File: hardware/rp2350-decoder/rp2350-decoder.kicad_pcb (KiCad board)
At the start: 6 copper layers, 19.9 x 8.8 mm, 67 parts, among them J1 SWDIO, J2 SWCLK, J3 5052702412, Q1 DMN2991UDA-7B, Q2 DMN2991UDA-7B, Q3 NST847BPDP6T5G, Q4 NST847BPDP6T5G, Q5 DMN2991UDA-7B, Q6 DMN2991UDA-7B, Q7 DMN2991UDA-7B, Q8 DMN2991UDA-7B, SW1 BOOT, U1 NCS2220AMUT1G, U2 AP63203WU, U3 W25Q128JVPIQ, U4 RP2350A, U5 MAX98357AEWL+T, U6 MD9927, Y1 X252012MMB4SI

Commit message: chore: increase bootsel resistance
chore: add missing heights
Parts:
- R6: value 1K -> 6.8K
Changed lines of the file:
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@@
 			)
 		)
-		(property "Frequency" ""
+		(property "Height" "1.0"
+			(at 0 0 -90)
+			(unlocked yes)
+			(layer "F.Fab")
+			(hide yes)
+			(effects
+				(font
+					(size 1 1)
+					(thickness 0.15)
+				)
+			)
+		)
+		(property "LCSC Part" "C42411119"
 			(at 0 0 -90)
 			(unlocked yes)
@@
 			)
 		)
+		(property "Height" "0.26"
+			(at 0 0 0)
+			(unlocked yes)
+			(layer "F.Fab")
+			(hide yes)
+			(effects
+				(font
+					(size 1 1)
+					(thickness 0.15)
+				)
+			)
+		)
 		(property ki_fp_filters "R_*")
 		(sheetname "Root")
@@
 			)
 		)
-		(property "Frequency" ""
+		(property "Height" "0.26"
 			(at 0 0 90)
 			(unlocked yes)
@@
 			)
 		)
+		(property "Height" "0.26"
+			(at 0 0 0)
+			(unlocked yes)
+			(layer "F.Fab")
+			(hide yes)
+			(effects
+				(font
+					(size 1 1)
+					(thickness 0.15)
+				)
+			)
+		)
 		(property ki_fp_filters "R_*")
 		(sheetname "Root")
@@
 			)
 		)
+		(property "Height" "0.26"
+			(at 0 0 0)
+			(unlocked yes)
+			(layer "F.Fab")
+			(hide yes)
+			(effects
+				(font
+					(size 1 1)
+					(thickness 0.15)
+				)
+			)
+		)
 		(property ki_fp_filters "R_*")
 		(sheetname "Root")
@@
 			)
 		)
+		(property "Height" "0.26"
+			(at 0 0 0)
+			(unlocked yes)
+			(layer "F.Fab")
+			(hide yes)
+			(effects
+				(font
+					(size 1 1)
+					(thickness 0.15)
+				)
+			)
+		)
 		(property ki_fp_filters "R_*")
 		(sheetname "Root")
@@
 			)
 		)
-		(property "Height" "0.7"
+		(property "Height" "0.55"
 			(at 0 0 90)
 			(unlocked yes)
@@
 			)
 		)
-		(property "Alternative Part" ""
-			(at 0 0 -90)
-			(unlocked yes)
-			(layer "F.Fab")
-			(hide yes)
-			(effects
-				(font
-					(size 1 1)
-					(thickness 0.15)
-				)
-			)
-		)
-		(property "Frequency" ""
-			(at 0 0 -90)
-			(unlocked yes)
-			(layer "F.Fab")
-			(hide yes)
-			(effects
-				(font
-					(size 1 1)
-					(thickness 0.15)
-				)
-			)
-		)
 		(property ki_fp_filters "C_*")
 		(sheetname "Root")
@@
 			)
 		)
+		(property "Height" "0.9"
+			(at 0 0 90)
+			(unlocked yes)
+			(layer "F.Fab")
+			(hide yes)
+			(effects
+				(font
+					(size 1 1)
+					(thickness 0.15)
+				)
+			)
+		)
 		(sheetname "Root")
 		(sheetfile "rp2350-decoder.kicad_sch")
@@
 			)
 		)
+		(property "Height" "0"
+			(at 0 0 180)
+			(unlocked yes)
+			(layer "B.Fab")
+			(hide yes)
+			(effects
+				(font
+					(size 1 1)
+					(thickness 0.15)
+				)
+				(justify mirror)
+			)
+		)
 		(property ki_fp_filters "Connector*:*_1x??_*")
 		(sheetname "Root")
@@
 			)
 		)
-		(property "Value" "1K"
+		(property "Value" "6.8K"
 			(at 0 -1.05 90)
 			(layer "B.Fab")
@@
 			)
 		)
-		(property "LCSC" "C270365"
+		(property "LCSC" "C423451"
 			(at 0 0 90)
 			(unlocked yes)
@@
 			)
 		)
-		(property "Frequency" ""
-			(at 0 0 -90)
-			(unlocked yes)
-			(layer "B.Fab")
-			(hide yes)
-			(effects
-				(font
-					(size 1 1)
-					(thickness 0.15)
-				)
-				(justify mirror)
-			)
-		)
 		(property ki_fp_filters "R_*")
 		(sheetname "Root")
@@
 			)
 		)
+		(property "Height" "0"
+			(at 0 0 180)
+			(unlocked yes)
+			(layer "B.Fab")
+			(hide yes)
+			(effects
+				(font
+					(size 1 1)
+					(thickness 0.15)
+				)
+				(justify mirror)
+			)
+		)
 		(property ki_fp_filters "Connector*:*_1x??_*")
 		(sheetname "Root")
@@
 			)
 		)
+		(property "Height" "0.4"
+			(at 0 0 180)
+			(unlocked yes)
+			(layer "B.Fab")
+			(hide yes)
+			(effects
+				(font
+					(size 1 1)
+					(thickness 0.15)
+				)
+				(justify mirror)
+			)
+		)
 		(property ki_fp_filters "SOT?363*")
 		(sheetname "Root")
@@
 			)
 		)
+		(property "Height" "0.4"
+			(at 0 0 180)
+			(unlocked yes)
+			(layer "B.Fab")
+			(hide yes)
+			(effects
+				(font
+					(size 1 1)
+					(thickness 0.15)
+				)
+				(justify mirror)
+			)
+		)
 		(property ki_fp_filters "SOT?363*")
 		(sheetname "Root")
@@
 			)
 		)
-		(property "Frequency" ""
+		(property "LCSC" "C270365"
 			(at 0 0 0)
 			(unlocked yes)
@@
 			)
 		)
-		(property "LCSC" "C270365"
-			(at 0 0 0)
+		(property "Height" "0.26"
+			(at 0 0 180)
 			(unlocked yes)
 			(layer "B.Fab")

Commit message: chore: add hardware revision and date codes
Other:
- board text added: "${REVISION}"
- board text removed: "E24 DCC"

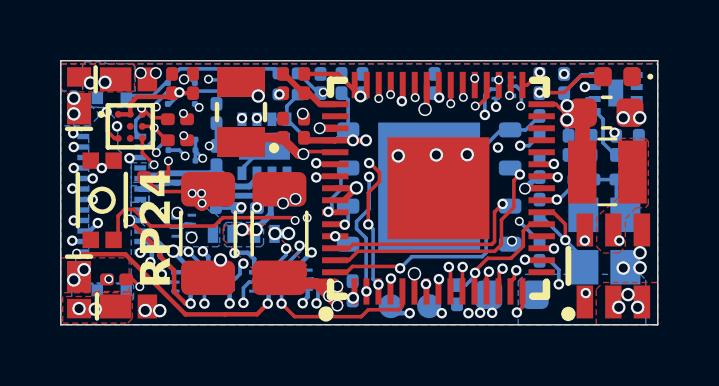
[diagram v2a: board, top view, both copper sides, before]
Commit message: fix: switch to recommended crystal
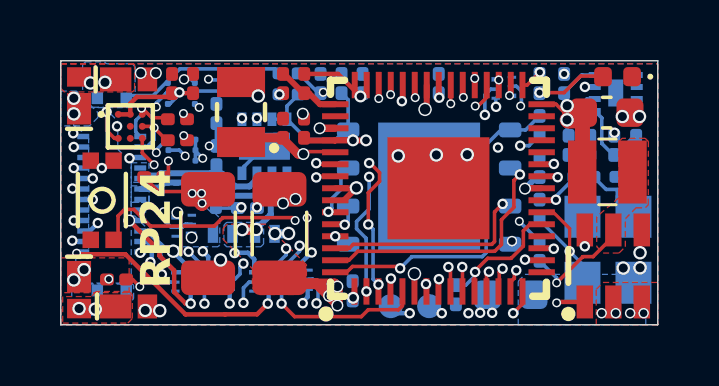
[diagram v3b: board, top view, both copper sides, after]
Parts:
- Y1: value X252012MMB4SI -> ABM8-272-T3; footprint Crystal:Crystal_SMD_2520-4Pin_2.5x2.0mm -> Crystal:Crystal_SMD_3225-4Pin_3.2x2.5mm
- moved Y1 0.31 mm to (118.2, 106.0), turned to 90 degrees
- moved C12 0.14 mm to (112.6, 100.5)
- moved C4 0.09 mm to (118.8, 103.6), turned to 180 degrees
- moved R2 0.09 mm to (119.2, 102.6), turned to -90 degrees
- moved R5 0.09 mm to (117.4, 103.6)
- moved R1 0.06 mm to (118.5, 102.6)
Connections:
- Y1 pad 1: Net-(C4-Pad1) -> /XIN
- Y1 pad 3: /XIN -> Net-(C4-Pad1)
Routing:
- net /XIN: track 3.22 -> 4.64 mm
- net Net-(C4-Pad1): track 1.63 -> 2.88 mm
- net +3.3V: track 29.6 -> 30.6 mm
- net /SWITCH: track 3.87 -> 3.72 mm, vias 2 -> 1
- net /CAP_VDC: vias 10 -> 11
